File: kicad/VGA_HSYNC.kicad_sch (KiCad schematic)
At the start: 14 parts, among them SW3 RESET, U19 74LS163, U2 74LS00, U20 74LS163, U21 74LS163, U22 74LS04, U23 74LS04, U24 74LS30, U25 74LS30, U26 74LS30, U27 74LS74

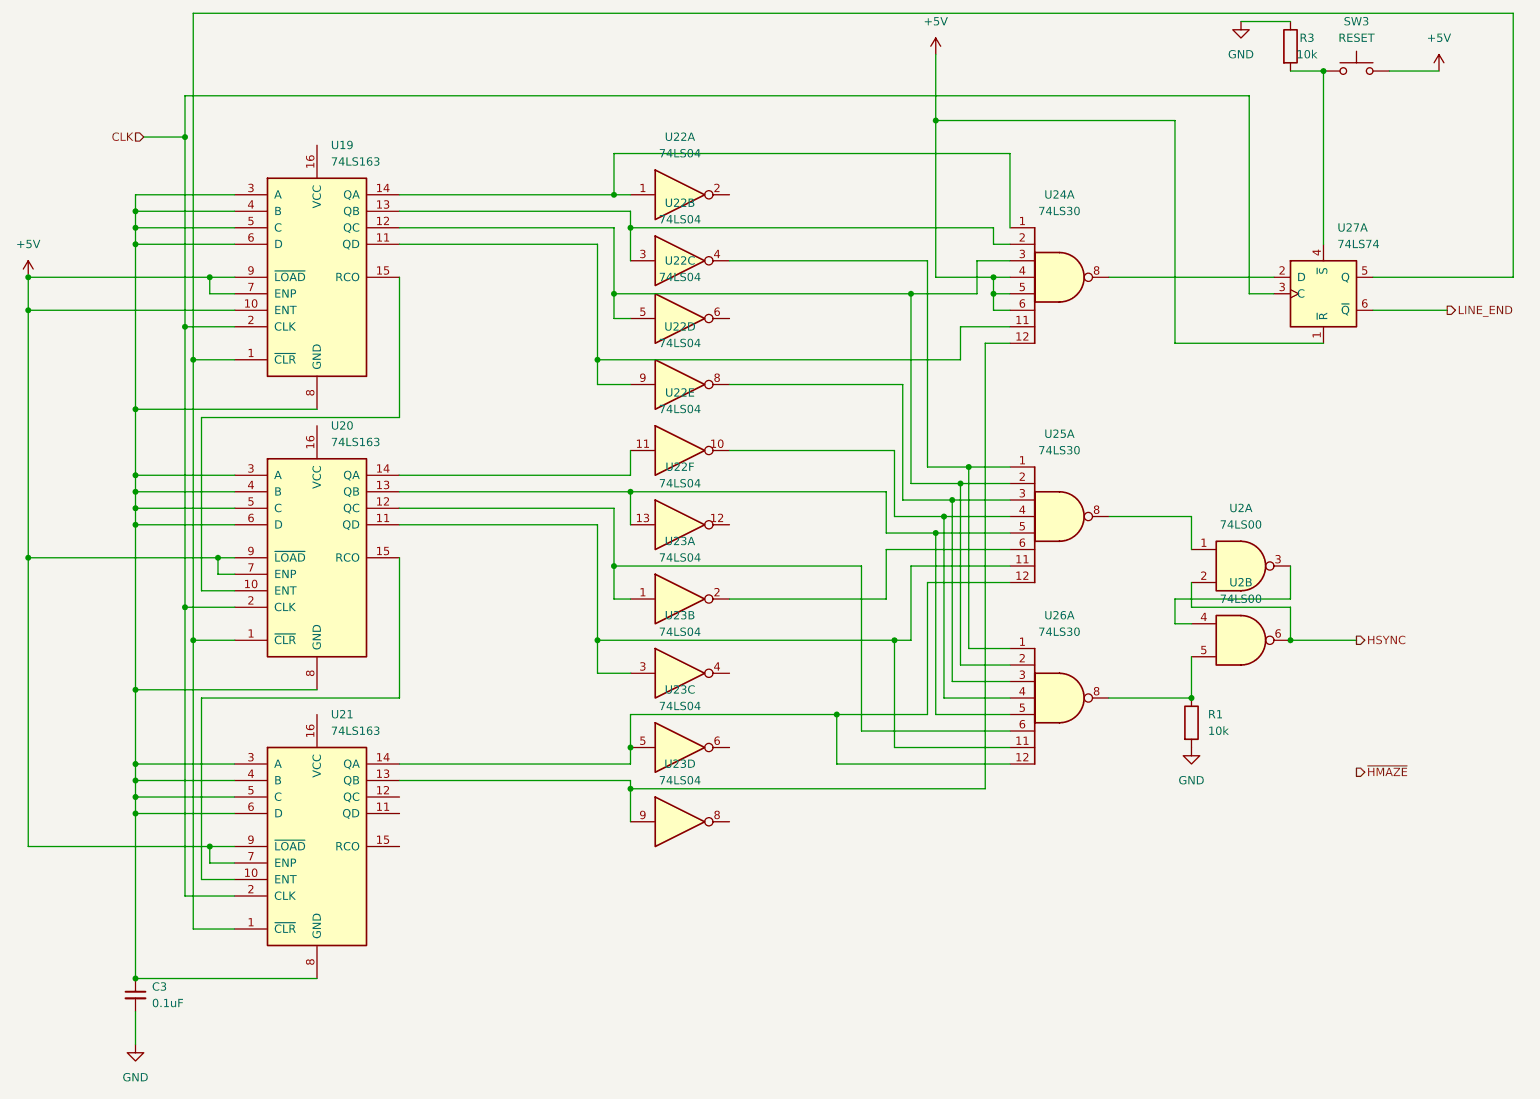
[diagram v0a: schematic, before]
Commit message: Add AT28C64 symbol. Tidy up HSYNC schematic. Add EEPROM - Z80 connection and VGA - Z80 connection
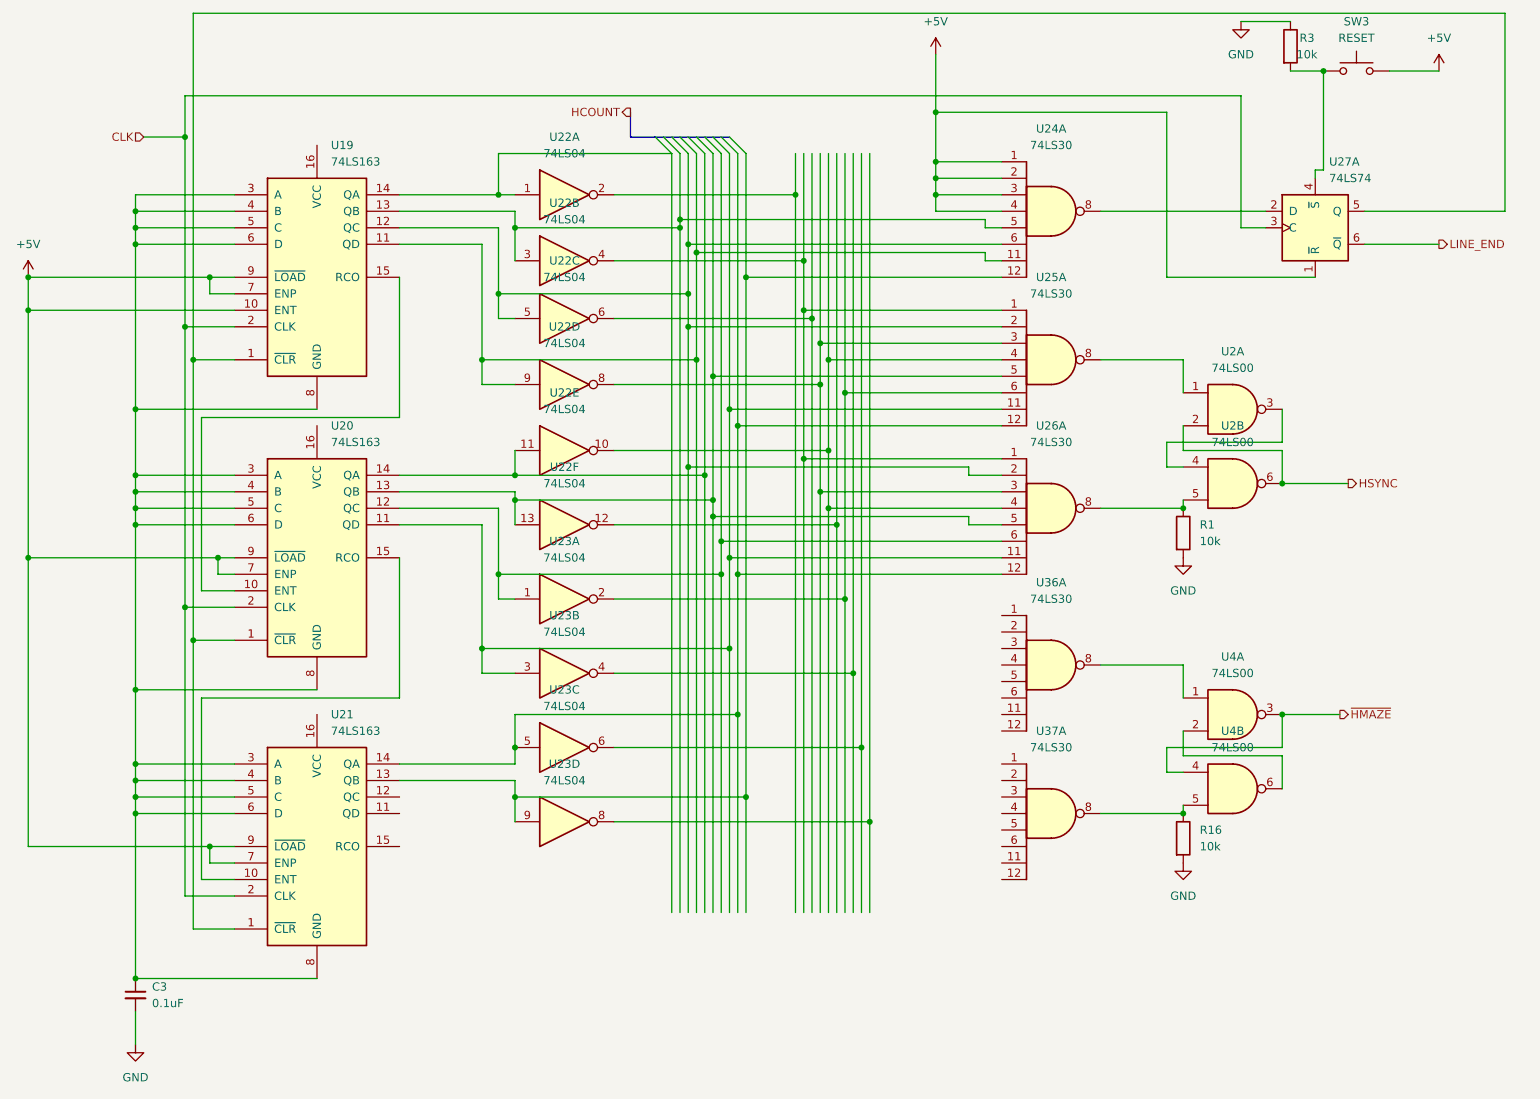
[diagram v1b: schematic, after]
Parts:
- added R16: 10k, symbol Device:R
- added U36, U37: 74LS30, symbol 74xx:74LS30
- added U4: 74LS00, symbol 74xx:74LS00
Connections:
- net +5V: now also U24.1, U24.2, U24.3; no longer U24.5, U24.6
- net GND: now also R16.2
- net ~{HMAZE}: now also U4.3, U4.4
- net at U19.12 (QC), U22.5, U25.2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: now also U24.6; no longer U24.3
- net at U19.14 (QA), U22.1: no longer U24.1
- net at U19.13 (QB), U22.3: now also U24.5; no longer U24.2
- new net: R16.1, U37.8, U4.5
- new net: U4.2, U4.6
- new net: U36.8, U4.1
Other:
- moved on the sheet: R1, U22A, U22B, U22C, U22D, U22E, U22F, U23A, U23B, U23C, U23D, U24A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
